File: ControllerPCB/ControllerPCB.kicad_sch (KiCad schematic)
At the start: 64 parts, among them J101 2x4 Pickup Conn, J102 1x4 String Output Conn, J103 Conn_01x03_Pin, J104 Conn_01x03_Pin, J105 Conn_01x03_Pin, J106 Conn_01x03_Pin, J107 USB_B_Micro, J108 10-pin Debug Conn, J109 Conn_01x03_Pin, U101 STM32F439ZIT6, Y101 16MHz

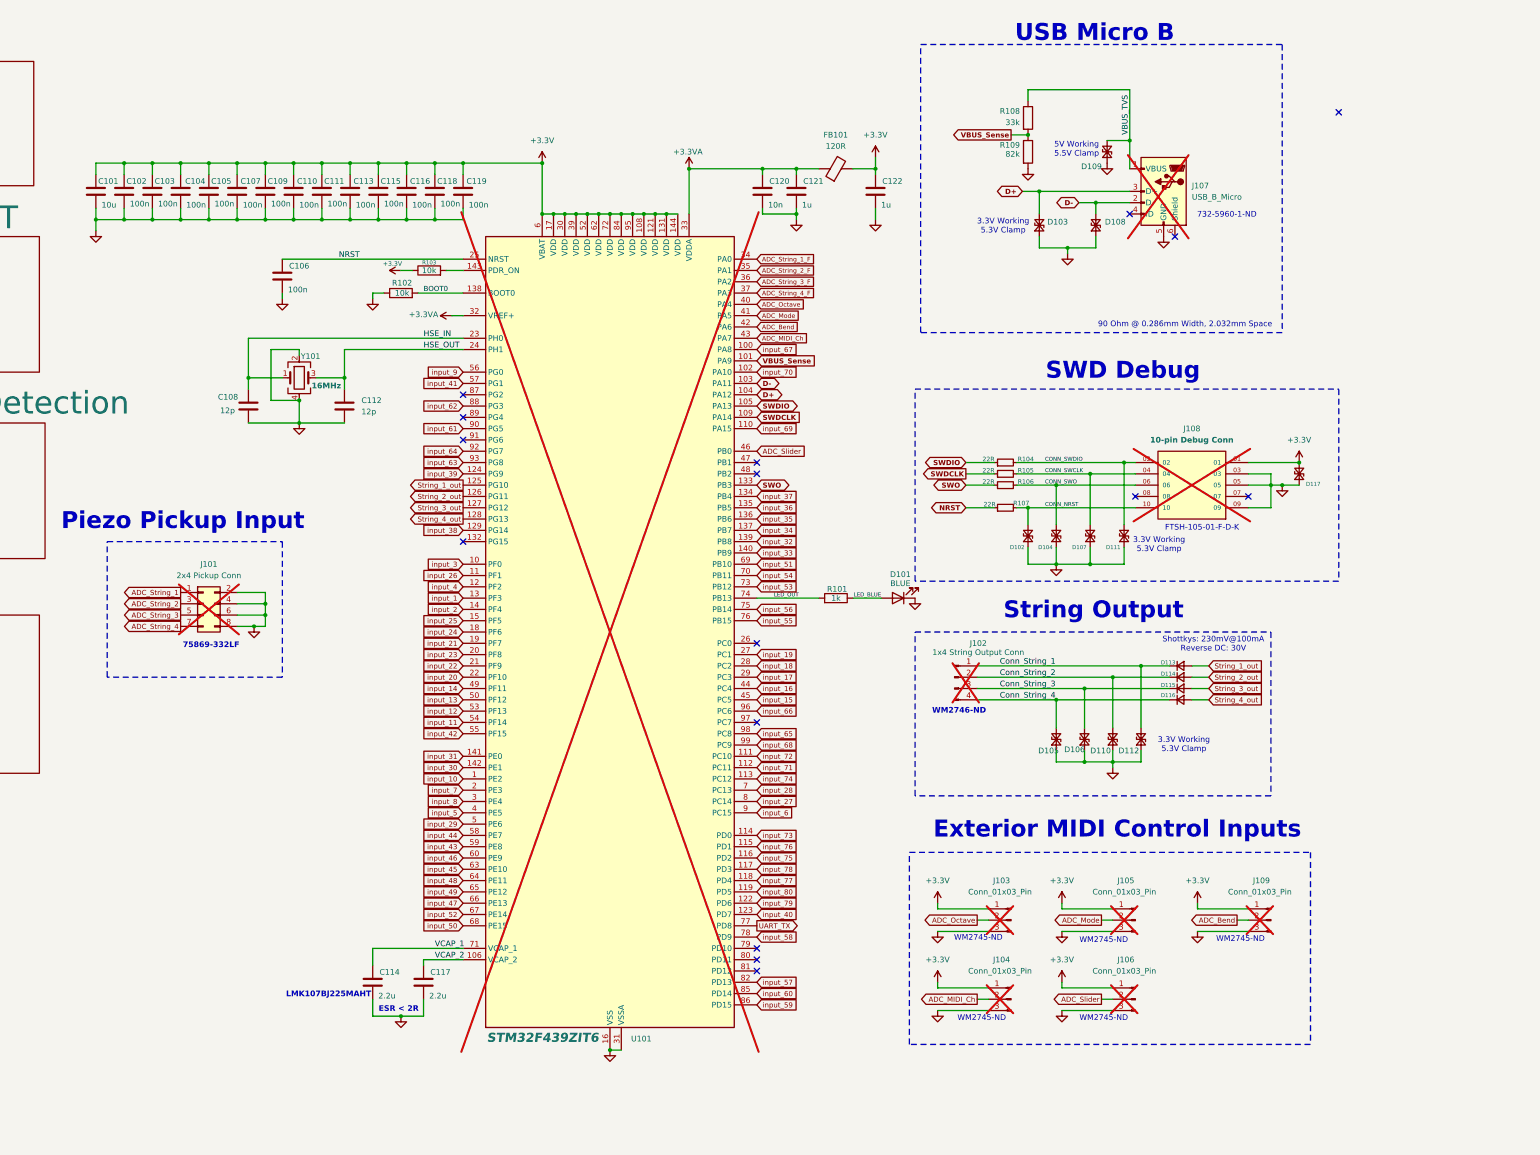
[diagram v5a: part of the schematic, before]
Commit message: rev 1.05
- new controller is used.
- updated the pcb layout
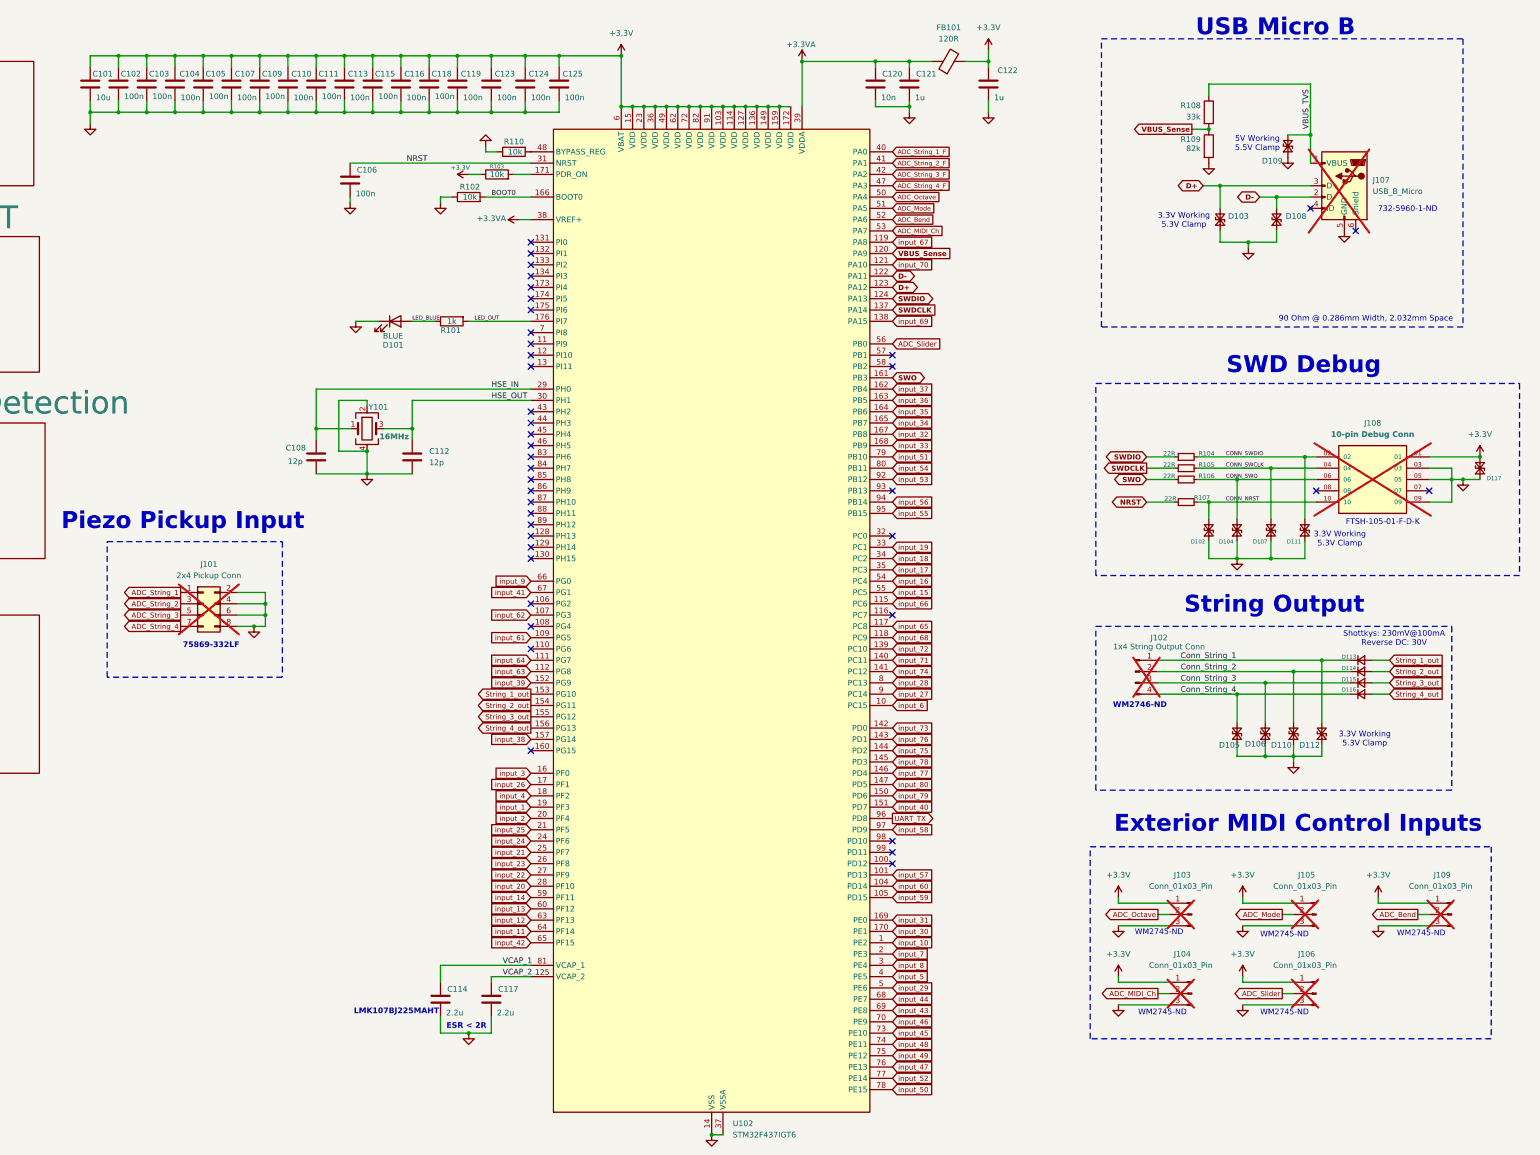
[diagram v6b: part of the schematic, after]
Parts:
- removed U101: STM32F439ZIT6, Package_QFP:LQFP-144_20x20mm_P0.5mm, symbol MCU_ST_STM32F4:STM32F439ZITx
- added C123, C124, C125: 100n, Capacitor_SMD:C_0402_1005Metric, symbol Device:C
- added R110: 10k, Resistor_SMD:R_0402_1005Metric, symbol Device:R
- added U102: STM32F437IGT6, Package_QFP:LQFP-176_24x24mm_P0.5mm, symbol MCU_ST_STM32F4:STM32F437IGTx
- R102, R103: footprint Resistor_SMD:R_1206_3216Metric -> Resistor_SMD:R_0402_1005Metric
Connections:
- net +3.3V: now also C123.1, C124.1, C125.1, U102.103 (VDD), U102.114 (VDD), U102.127 (VDD), U102.136 (VDD), U102.149 (VDD), U102.15 (VDD), U102.159 (VDD), U102.172 (VDD), U102.23 (VDD), U102.36 (VDD), U102.49 (VDD), U102.6 (VBAT), U102.62 (VDD), U102.72 (VDD), U102.82 (VDD), U102.91 (VDD)
- net +3.3VA: now also U102.38 (VREF+), U102.39 (VDDA)
- net ADC_Bend: now also U102.52 (PA6)
- net ADC_MIDI_Ch: now also U102.53 (PA7)
- net ADC_Mode: now also U102.51 (PA5)
- net ADC_Octave: now also U102.50 (PA4)
- net ADC_Slider: now also U102.56 (PB0)
- net ADC_String_1_F: now also U102.40 (PA0)
- net ADC_String_2_F: now also U102.41 (PA1)
- net ADC_String_3_F: now also U102.42 (PA2)
- net ADC_String_4_F: now also U102.47 (PA3)
- net BOOT0: now also U102.166 (BOOT0)
- net D+: now also U102.123 (PA12)
- net D-: now also U102.122 (PA11)
- net GND: now also C123.2, C124.2, C125.2, R110.1, U102.102 (VSS), U102.113 (VSS), U102.126 (VSS), U102.135 (VSS), U102.14 (VSS), U102.148 (VSS), U102.158 (VSS), U102.22 (VSS), U102.37 (VSSA), U102.61 (VSS), U102.71 (VSS), U102.90 (VSS)
- net HSE_IN: now also U102.29 (PH0)
- net HSE_OUT: now also U102.30 (PH1)
- net LED_OUT: now also U102.176 (PI7)
- net NRST: now also U102.31 (NRST)
- net SWDCLK: now also U102.137 (PA14)
- net SWDIO: now also U102.124 (PA13)
- net SWO: now also U102.161 (PB3)
- net String_1_out: now also U102.153 (PG10)
- net String_2_out: now also U102.154 (PG11)
- net String_3_out: now also U102.155 (PG12)
- net String_4_out: now also U102.156 (PG13)
- net UART_TX: now also U102.96 (PD8)
- net VBUS_Sense: now also U102.120 (PA9)
- net VCAP_1: now also U102.81 (VCAP_1)
- net VCAP_2: now also U102.125 (VCAP_2)
- net input_1: now also U102.19 (PF3)
- net input_10: now also U102.1 (PE2)
- net input_11: now also U102.64 (PF14)
- net input_12: now also U102.63 (PF13)
- net input_13: now also U102.60 (PF12)
- net input_14: now also U102.59 (PF11)
- net input_15: now also U102.55 (PC5)
- net input_16: now also U102.54 (PC4)
- net input_17: now also U102.35 (PC3)
- net input_18: now also U102.34 (PC2)
- net input_19: now also U102.33 (PC1)
- net input_2: now also U102.20 (PF4)
- net input_20: now also U102.28 (PF10)
- net input_21: now also U102.25 (PF7)
- net input_22: now also U102.27 (PF9)
- net input_23: now also U102.26 (PF8)
- net input_24: now also U102.24 (PF6)
- net input_25: now also U102.21 (PF5)
- net input_26: now also U102.17 (PF1)
- net input_27: now also U102.9 (PC14)
- net input_28: now also U102.8 (PC13)
- net input_29: now also U102.5 (PE6)
- net input_3: now also U102.16 (PF0)
- net input_30: now also U102.170 (PE1)
- net input_31: now also U102.169 (PE0)
- net input_32: now also U102.167 (PB8)
- net input_33: now also U102.168 (PB9)
- net input_34: now also U102.165 (PB7)
- net input_35: now also U102.164 (PB6)
- net input_36: now also U102.163 (PB5)
- net input_37: now also U102.162 (PB4)
- net input_38: now also U102.157 (PG14)
- net input_39: now also U102.152 (PG9)
- net input_4: now also U102.18 (PF2)
- net input_40: now also U102.151 (PD7)
- net input_41: now also U102.67 (PG1)
- net input_42: now also U102.65 (PF15)
- net input_43: now also U102.69 (PE8)
- net input_44: now also U102.68 (PE7)
- net input_45: now also U102.73 (PE10)
- net input_46: now also U102.70 (PE9)
- net input_47: now also U102.76 (PE13)
- net input_48: now also U102.74 (PE11)
- net input_49: now also U102.75 (PE12)
- net input_5: now also U102.4 (PE5)
- net input_50: now also U102.78 (PE15)
- net input_51: now also U102.79 (PB10)
- net input_52: now also U102.77 (PE14)
- net input_53: now also U102.92 (PB12)
- net input_54: now also U102.80 (PB11)
- net input_55: now also U102.95 (PB15)
- net input_56: now also U102.94 (PB14)
- net input_57: now also U102.101 (PD13)
- net input_58: now also U102.97 (PD9)
- net input_59: now also U102.105 (PD15)
- net input_6: now also U102.10 (PC15)
- net input_60: now also U102.104 (PD14)
- net input_61: now also U102.109 (PG5)
- net input_62: now also U102.107 (PG3)
- net input_63: now also U102.112 (PG8)
- net input_64: now also U102.111 (PG7)
- net input_65: now also U102.117 (PC8)
- net input_66: now also U102.115 (PC6)
- net input_67: now also U102.119 (PA8)
- net input_68: now also U102.118 (PC9)
- net input_69: now also U102.138 (PA15)
- net input_7: now also U102.2 (PE3)
- net input_70: now also U102.121 (PA10)
- net input_71: now also U102.140 (PC11)
- net input_72: now also U102.139 (PC10)
- net input_73: now also U102.142 (PD0)
- net input_74: now also U102.141 (PC12)
- net input_75: now also U102.144 (PD2)
- net input_76: now also U102.143 (PD1)
- net input_77: now also U102.146 (PD4)
- net input_78: now also U102.145 (PD3)
- net input_79: now also U102.150 (PD6)
- net input_8: now also U102.3 (PE4)
- net input_80: now also U102.147 (PD5)
- net input_9: now also U102.66 (PG0)
- net at R103.2: now also U102.171 (PDR_ON)
- new net: R110.2, U102.48 (BYPASS_REG)
- no-connect marks 16 -> 41
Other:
- moved on the sheet: C101, C102, C103, C104, C105, C106, C107, C108, C109, C110, C111, C112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
